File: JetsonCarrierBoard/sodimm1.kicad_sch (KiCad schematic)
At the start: 10 parts

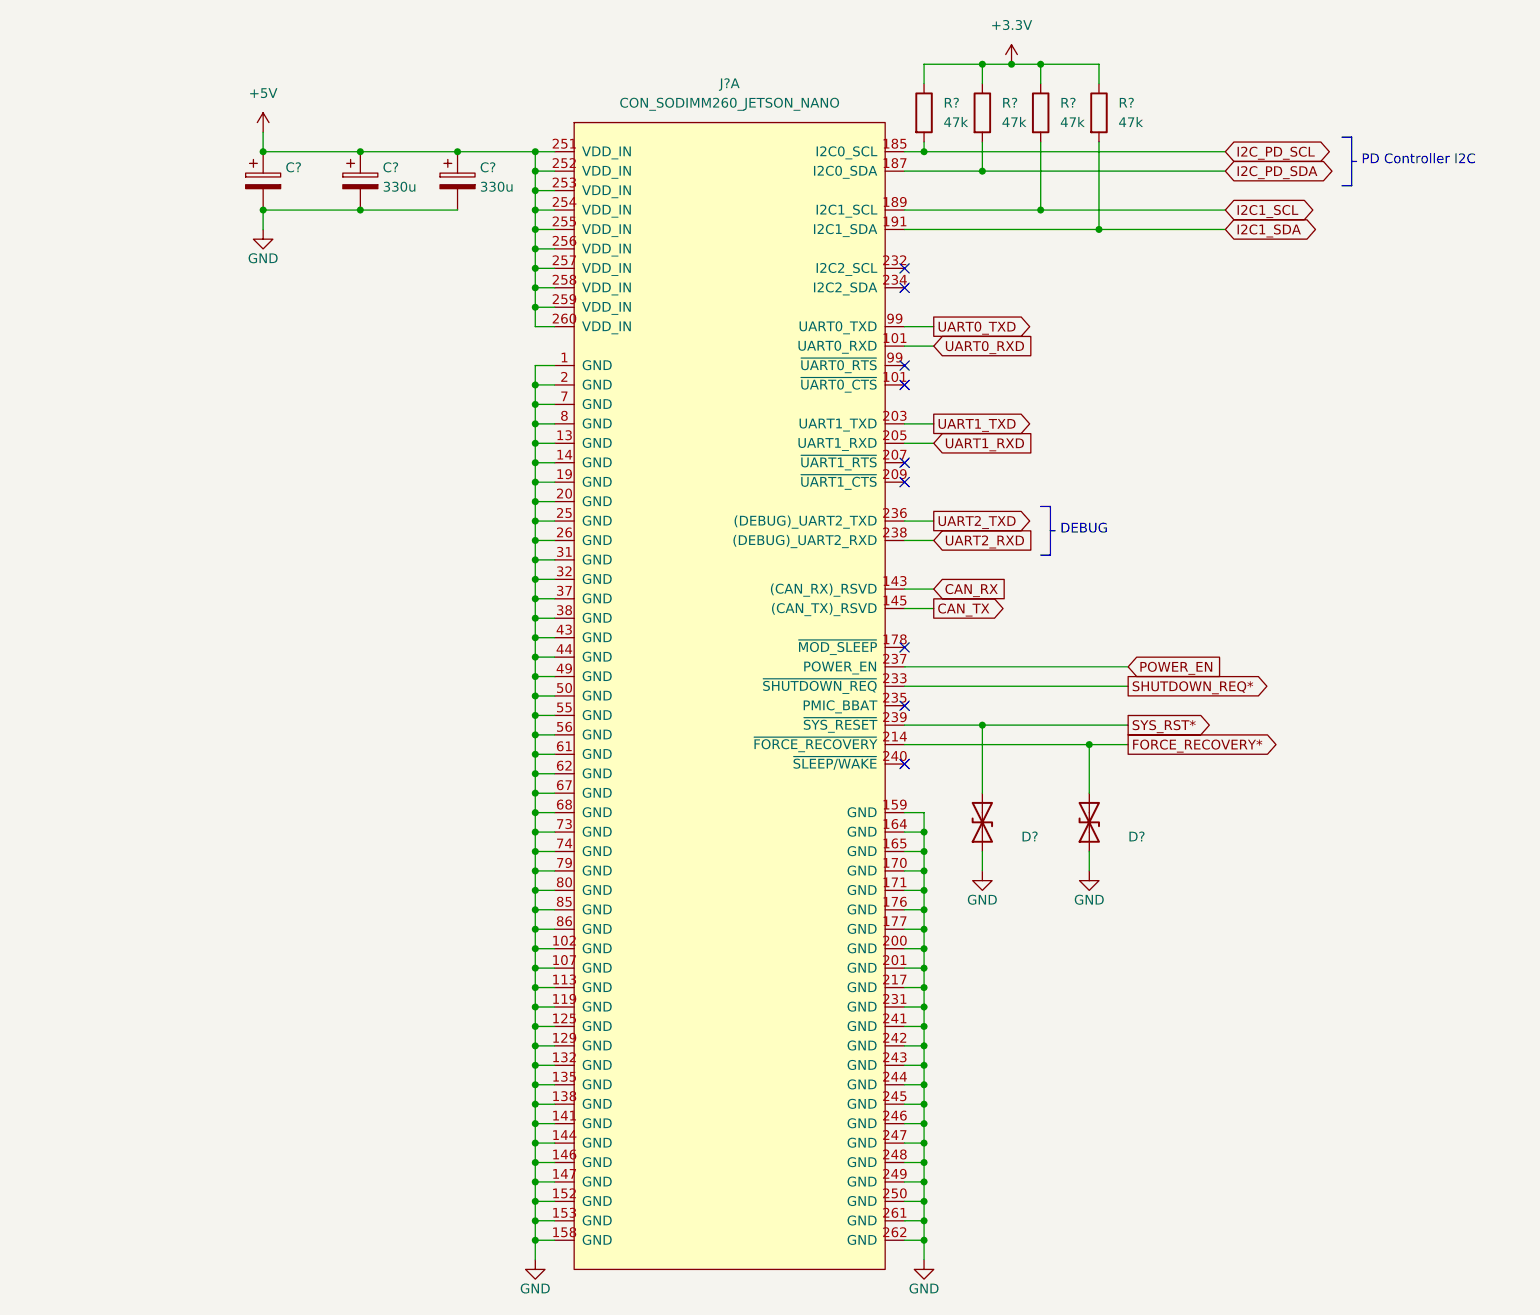
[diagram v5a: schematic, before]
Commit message: Improvement list, fixes, and readability improvements
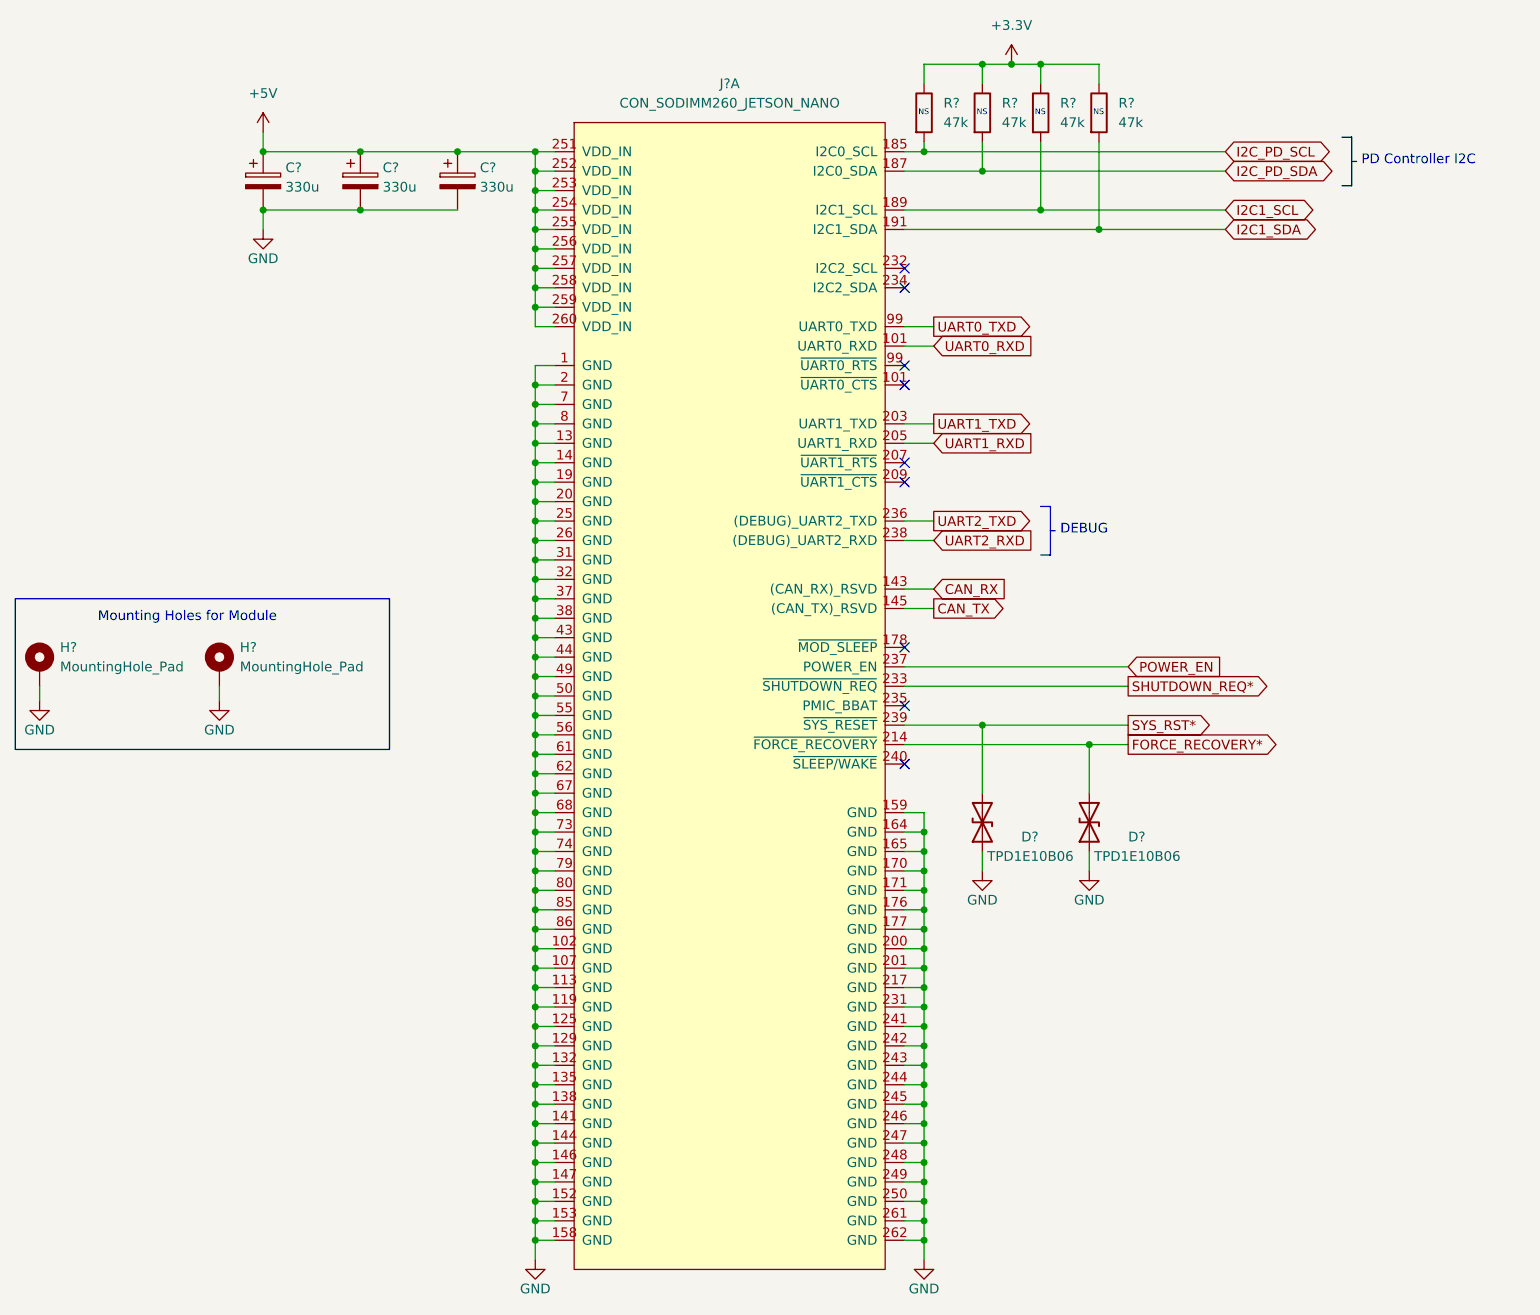
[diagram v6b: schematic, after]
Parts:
- added H? (x2): MountingHole_Pad, symbol Mechanical:MountingHole_Pad
- C?: value (none) -> 330u
- D? (x2): value (none) -> TPD1E10B06
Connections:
- net GND: now also H?.1, H?.1
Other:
- note added: "Mounting Holes for Module"
- note added: "NS"
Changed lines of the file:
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@@
     (stroke (width 0) (type default) (color 0 0 0 0))
+  )
+  (polyline (pts (xy 51.435 91.44) (xy 100.33 91.44))
+    (stroke (width 0) (type solid) (color 0 0 0 1))
   )
   (wire (pts (xy 119.38 76.2) (xy 121.92 76.2))
@@
     (stroke (width 0) (type default) (color 0 0 0 0))
   )
+  (polyline (pts (xy 51.435 91.44) (xy 51.435 111.125))
+    (stroke (width 0) (type solid) (color 0 0 0 1))
+  )
   (wire (pts (xy 170.18 160.02) (xy 170.18 162.56))
     (stroke (width 0) (type default) (color 0 0 0 0))
@@
     (stroke (width 0) (type default) (color 0 0 0 0))
   )
+  (polyline (pts (xy 100.33 91.44) (xy 100.33 111.125))
+    (stroke (width 0) (type solid) (color 0 0 0 1))
+  )
   (wire (pts (xy 119.38 162.56) (xy 119.38 165.1))
     (stroke (width 0) (type default) (color 0 0 0 0))
@@
     (stroke (width 0) (type default) (color 0 0 0 0))
   )
+  (wire (pts (xy 54.61 102.87) (xy 54.61 104.775))
+    (stroke (width 0) (type default) (color 0 0 0 0))
+  )
   (wire (pts (xy 119.38 68.58) (xy 121.92 68.58))
     (stroke (width 0) (type default) (color 0 0 0 0))
@@
   (wire (pts (xy 119.38 175.26) (xy 119.38 177.8))
     (stroke (width 0) (type default) (color 0 0 0 0))
+  )
+  (polyline (pts (xy 100.33 111.125) (xy 51.435 111.125))
+    (stroke (width 0) (type solid) (color 0 0 0 1))
   )
   (wire (pts (xy 83.82 33.02) (xy 96.52 33.02))
@@
     (stroke (width 0) (type default) (color 0 0 0 0))
   )
+  (wire (pts (xy 78.105 102.87) (xy 78.105 104.775))
+    (stroke (width 0) (type default) (color 0 0 0 0))
+  )
   (wire (pts (xy 167.64 119.38) (xy 170.18 119.38))
     (stroke (width 0) (type default) (color 0 0 0 0))
@@
     (stroke (width 0) (type default) (color 0 0 0 0))
   )
+  (text "NS" (at 184.658 28.448 0)
+    (effects (font (size 0.75 0.75)) (justify left bottom))
+  )
+  (text "NS" (at 177.038 28.448 0)
+    (effects (font (size 0.75 0.75)) (justify left bottom))
+  )
+  (text "NS" (at 169.418 28.448 0)
+    (effects (font (size 0.75 0.75)) (justify left bottom))
+  )
   (text "DEBUG" (at 187.96 83.185 0)
     (effects (font (size 1.27 1.27)) (justify left bottom))
@@
     (effects (font (size 1.27 1.27)) (justify left bottom))
   )
+  (text "NS" (at 192.278 28.448 0)
+    (effects (font (size 0.75 0.75)) (justify left bottom))
+  )
+  (text "Mounting Holes for Module" (at 62.23 94.615 0)
+    (effects (font (size 1.27 1.27)) (justify left bottom))
+  )
   (global_label "I2C1_SDA" (shape bidirectional) (at 209.55 43.18 0) (fields_autoplaced)
     (effects (font (size 1.27 1.27)) (justify left))
@@
       (effects (font (size 1.27 1.27)) (justify left) hide)
     )
+  )
+  (symbol (lib_id "Mechanical:MountingHole_Pad") (at 54.61 100.33 0) (unit 1)
+    (in_bom yes) (on_board yes) (fields_autoplaced)
+    (property "Reference" "H?" (id 0) (at 57.277 97.7899 0)
+      (effects (font (size 1.27 1.27)) (justify left))
+    )
+    (property "Value" "MountingHole_Pad" (id 1) (at 57.277 100.3299 0)
+      (effects (font (size 1.27 1.27)) (justify left))
+    )
+    (property "Footprint" "" (id 2) (at 54.61 100.33 0)
+      (effects (font (size 1.27 1.27)) hide)
+    )
+    (property "Datasheet" "~" (id 3) (at 54.61 100.33 0)
+      (effects (font (size 1.27 1.27)) hide)
+    )
+    (pin "1")
   )
   (symbol (lib_id "power:GND") (at 119.38 177.8 0) (unit 1)
@@
     )
     (property "Datasheet" "" (id 3) (at 119.38 177.8 0)
+      (effects (font (size 1.27 1.27)) hide)
+    )
+    (pin "1")
+  )
+  (symbol (lib_id "Mechanical:MountingHole_Pad") (at 78.105 100.33 0) (unit 1)
+    (in_bom yes) (on_board yes) (fields_autoplaced)
+    (property "Reference" "H?" (id 0) (at 80.772 97.7899 0)
+      (effects (font (size 1.27 1.27)) (justify left))
+    )
+    (property "Value" "MountingHole_Pad" (id 1) (at 80.772 100.3299 0)
+      (effects (font (size 1.27 1.27)) (justify left))
+    )
+    (property "Footprint" "" (id 2) (at 78.105 100.33 0)
+      (effects (font (size 1.27 1.27)) hide)
+    )
+    (property "Datasheet" "~" (id 3) (at 78.105 100.33 0)
       (effects (font (size 1.27 1.27)) hide)
     )
@@
       (effects (font (size 1.27 1.27)) (justify right))
     )
-    (property "Value" "" (id 1) (at 192.405 125.095 90)
+    (property "Value" "TPD1E10B06" (id 1) (at 192.405 125.095 90)
       (effects (font (size 1.27 1.27)) (justify right))
     )
@@
       (effects (font (size 1.27 1.27)) (justify left))
     )
-    (property "Value" "" (id 1) (at 86.741 37.6432 0)
+    (property "Value" "330u" (id 1) (at 86.741 37.6432 0)
       (effects (font (size 1.27 1.27)) (justify left))
     )
@@
     (pin "1")
     (pin "2")
+  )
+  (symbol (lib_id "power:GND") (at 78.105 104.775 0) (unit 1)
+    (in_bom yes) (on_board yes)
+    (property "Reference" "#PWR?" (id 0) (at 78.105 111.125 0)
+      (effects (font (size 1.27 1.27)) hide)
+    )
+    (property "Value" "GND" (id 1) (at 78.105 108.585 0))
+    (property "Footprint" "" (id 2) (at 78.105 104.775 0)
+      (effects (font (size 1.27 1.27)) hide)
+    )
+    (property "Datasheet" "" (id 3) (at 78.105 104.775 0)
+      (effects (font (size 1.27 1.27)) hide)
+    )
+    (pin "1")
   )
   (symbol (lib_id "power:GND") (at 170.18 177.8 0) (unit 1)
@@
     (pin "1")
     (pin "2")
+  )
+  (symbol (lib_id "power:GND") (at 54.61 104.775 0) (unit 1)
+    (in_bom yes) (on_board yes)
+    (property "Reference" "#PWR?" (id 0) (at 54.61 111.125 0)
+      (effects (font (size 1.27 1.27)) hide)
+    )
+    (property "Value" "GND" (id 1) (at 54.61 108.585 0))
+    (property "Footprint" "" (id 2) (at 54.61 104.775 0)
+      (effects (font (size 1.27 1.27)) hide)
+    )
+    (property "Datasheet" "" (id 3) (at 54.61 104.775 0)
+      (effects (font (size 1.27 1.27)) hide)
+    )
+    (pin "1")
   )
   (symbol (lib_id "Device:R") (at 170.18 27.94 0) (unit 1)
@@
       (effects (font (size 1.27 1.27)) (justify right))
     )
-    (property "Value" "" (id 1) (at 178.435 125.095 90)
+    (property "Value" "TPD1E10B06" (id 1) (at 178.435 125.095 90)
       (effects (font (size 1.27 1.27)) (justify right))
     )
